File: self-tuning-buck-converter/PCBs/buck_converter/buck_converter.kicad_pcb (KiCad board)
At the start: 2 copper layers, 3 parts, among them U4 ESP32-DEVKITC-32D

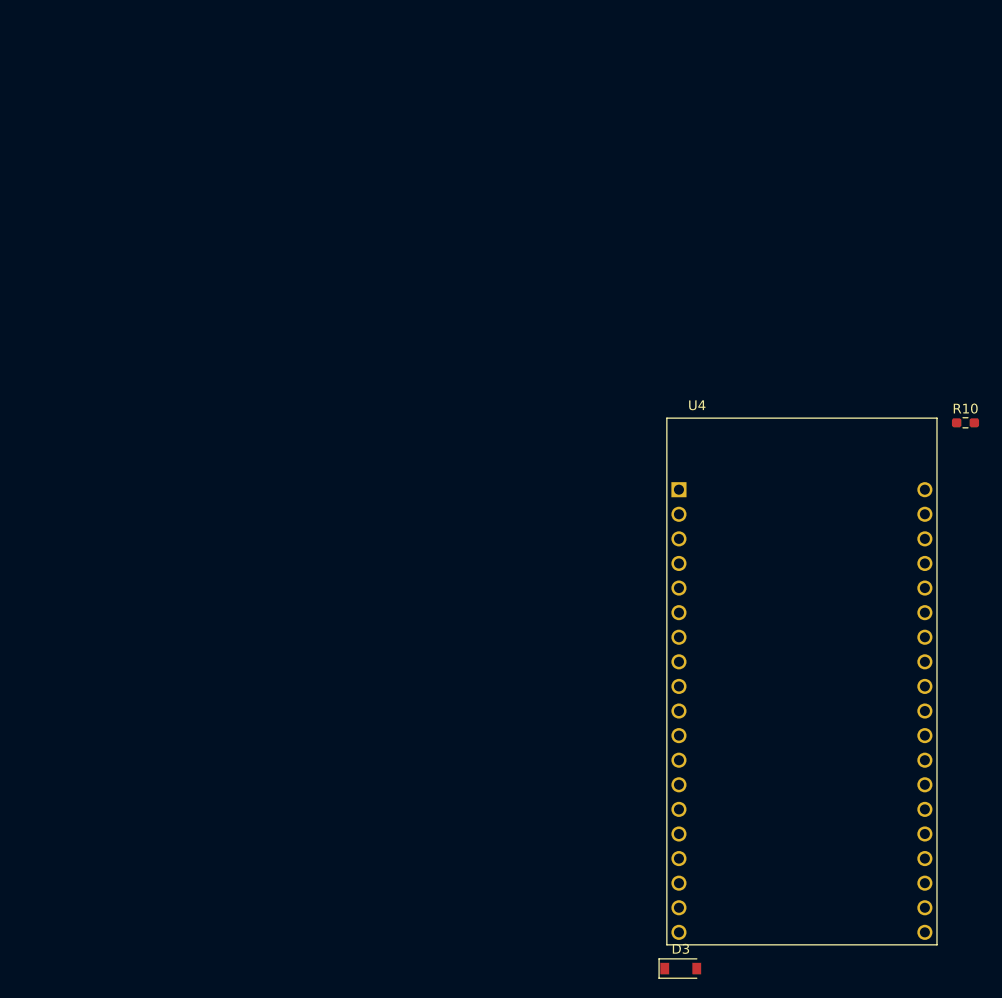
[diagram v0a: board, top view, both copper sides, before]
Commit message: Finalised PCM and selected component footprints
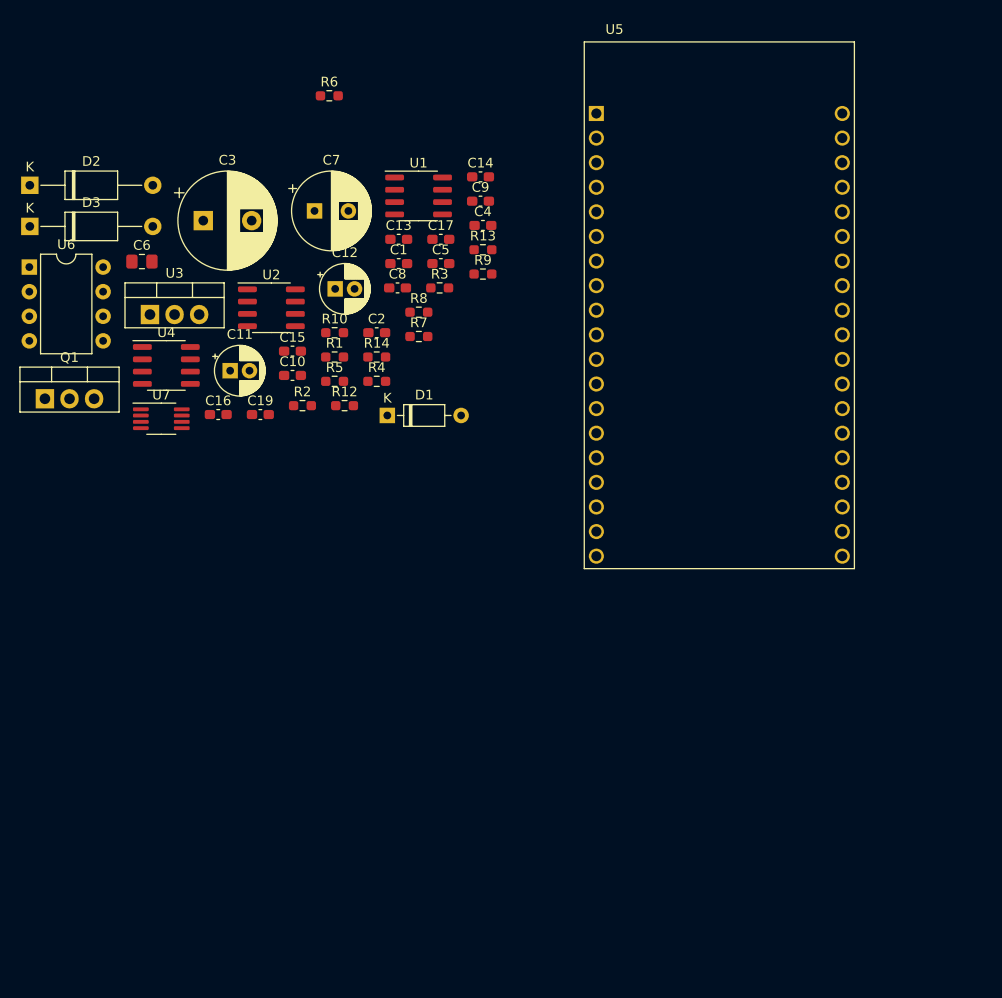
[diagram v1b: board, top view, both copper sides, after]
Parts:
- added C1: 0.1u 16V, Capacitor_SMD:C_0603_1608Metric_Pad1.08x0.95mm_HandSolder, F.Cu at (-33.1, -47.4)
- added C10: 1u 16V, Capacitor_SMD:C_0603_1608Metric_Pad1.08x0.95mm_HandSolder, F.Cu at (-44.1, -35.9)
- added C11: 10u 50V, Capacitor_THT:CP_Radial_D5.0mm_P2.00mm, F.Cu at (-50.5, -36.4)
- added C12: 10u 50V, Capacitor_THT:CP_Radial_D5.0mm_P2.00mm, F.Cu at (-39.7, -44.8)
- added C13: 0.1u 16V, Capacitor_SMD:C_0603_1608Metric_Pad1.08x0.95mm_HandSolder, F.Cu at (-33.1, -49.9)
- added C14: 0.1u 16V, Capacitor_SMD:C_0603_1608Metric_Pad1.08x0.95mm_HandSolder, F.Cu at (-24.7, -56.4)
- added C15: 0.1u 16V, Capacitor_SMD:C_0603_1608Metric_Pad1.08x0.95mm_HandSolder, F.Cu at (-44.1, -38.4)
- added C16: 0.1u 16V, Capacitor_SMD:C_0603_1608Metric_Pad1.08x0.95mm_HandSolder, F.Cu at (-51.8, -31.8)
- added C17: 4.7u 16V, Capacitor_SMD:C_0603_1608Metric_Pad1.08x0.95mm_HandSolder, F.Cu at (-28.8, -49.9)
- added C19: 0.1u 16V, Capacitor_SMD:C_0603_1608Metric_Pad1.08x0.95mm_HandSolder, F.Cu at (-47.4, -31.8)
- added C2: 0.1u 16V, Capacitor_SMD:C_0603_1608Metric_Pad1.08x0.95mm_HandSolder, F.Cu at (-35.4, -40.3)
- added C3: 100u 50V, Capacitor_THT:CP_Radial_D10.0mm_P5.00mm, F.Cu at (-53.3, -51.9)
- added C4: 0.1u 16V, Capacitor_SMD:C_0603_1608Metric_Pad1.08x0.95mm_HandSolder, F.Cu at (-24.4, -51.4)
- added C5: 100n 16V, Capacitor_SMD:C_0603_1608Metric_Pad1.08x0.95mm_HandSolder, F.Cu at (-28.8, -47.4)
- added C6: 10u 16V, Capacitor_SMD:C_0805_2012Metric_Pad1.18x1.45mm_HandSolder, F.Cu at (-59.6, -47.6)
- added C7: 100u 16V, Capacitor_THT:CP_Radial_D8.0mm_P3.50mm, F.Cu at (-41.8, -52.9)
- added C8: 0.1u 16V, Capacitor_SMD:C_0603_1608Metric_Pad1.08x0.95mm_HandSolder, F.Cu at (-33.2, -44.9)
- added C9: 10n 16V, Capacitor_SMD:C_0603_1608Metric_Pad1.08x0.95mm_HandSolder, F.Cu at (-24.7, -53.9)
- added D2: D_Schottky, Diode_THT:D_A-405_P12.70mm_Horizontal, F.Cu at (-71.2, -55.5)
- added D3: D_Schottky, Diode_THT:D_A-405_P12.70mm_Horizontal, F.Cu at (-71.2, -51.3)
- added Q1: NMOS, Package_TO_SOT_THT:TO-220-3_Vertical, F.Cu at (-69.7, -33.5)
- added R1: 100k, Resistor_SMD:R_0603_1608Metric_Pad0.98x0.95mm_HandSolder, F.Cu at (-39.7, -37.8)
- added R10: 120k, Resistor_SMD:R_0603_1608Metric_Pad0.98x0.95mm_HandSolder, F.Cu at (-39.7, -40.3)
- added R12: 5, Resistor_SMD:R_0603_1608Metric_Pad0.98x0.95mm_HandSolder, F.Cu at (-38.7, -32.8)
- added R13: 56k, Resistor_SMD:R_0603_1608Metric_Pad0.98x0.95mm_HandSolder, F.Cu at (-24.4, -48.9)
- added R14: 22k, Resistor_SMD:R_0603_1608Metric_Pad0.98x0.95mm_HandSolder, F.Cu at (-35.4, -37.8)
- added R2: 100k, Resistor_SMD:R_0603_1608Metric_Pad0.98x0.95mm_HandSolder, F.Cu at (-43.1, -32.8)
- added R3: 10k, Resistor_SMD:R_0603_1608Metric_Pad0.98x0.95mm_HandSolder, F.Cu at (-28.9, -44.9)
- added R4: 33, Resistor_SMD:R_0603_1608Metric_Pad0.98x0.95mm_HandSolder, F.Cu at (-35.4, -35.3)
- added R5: 1M, Resistor_SMD:R_0603_1608Metric_Pad0.98x0.95mm_HandSolder, F.Cu at (-39.7, -35.3)
- added R7: 10, Resistor_SMD:R_0603_1608Metric_Pad0.98x0.95mm_HandSolder, F.Cu at (-31.0, -39.9)
- added R8: 2k, Resistor_SMD:R_0603_1608Metric_Pad0.98x0.95mm_HandSolder, F.Cu at (-31.0, -42.4)
- added R9: 560k, Resistor_SMD:R_0603_1608Metric_Pad0.98x0.95mm_HandSolder, F.Cu at (-24.4, -46.4)
- added U1: LM7322, Package_SO:SOIC-8_3.9x4.9mm_P1.27mm, F.Cu at (-31.1, -54.4)
- added U2: LM7322, Package_SO:SOIC-8_3.9x4.9mm_P1.27mm, F.Cu at (-46.3, -42.9)
- added U3: LD1117V50, Package_TO_SOT_THT:TO-220-3_Vertical, F.Cu at (-58.8, -42.2)
- added U4: LT1999-50, Package_SO:SOIC-8_3.9x4.9mm_P1.27mm, F.Cu at (-57.1, -36.9)
- added U6: IR2125, Package_DIP:DIP-8_W7.62mm, F.Cu at (-71.3, -47.1)
- added U7: MAX11644, Package_SO:MSOP-8_3x3mm_P0.65mm, F.Cu at (-57.6, -31.4)
- D1: renamed from D3; footprint Diode_SMD:D_SOD-123 -> Diode_THT:D_DO-35_SOD27_P7.62mm_Horizontal
- moved R6 73.9 mm to (-40.3, -64.8)
- moved D1 64.7 mm to (-34.3, -31.8)
- moved U5 39.8 mm to (0.00, -43.2)
- renumbered R10 to R6, U4 to U5
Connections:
- U5 pad 10: Net-(U4-Pad10) -> SCL
- U5 pad 19: Net-(U4-Pad19) -> +5V
- U5 pad 5: Net-(U4-Pad5) -> Avg_voltage
- U5 pad 9: Net-(U4-Pad9) -> SDA

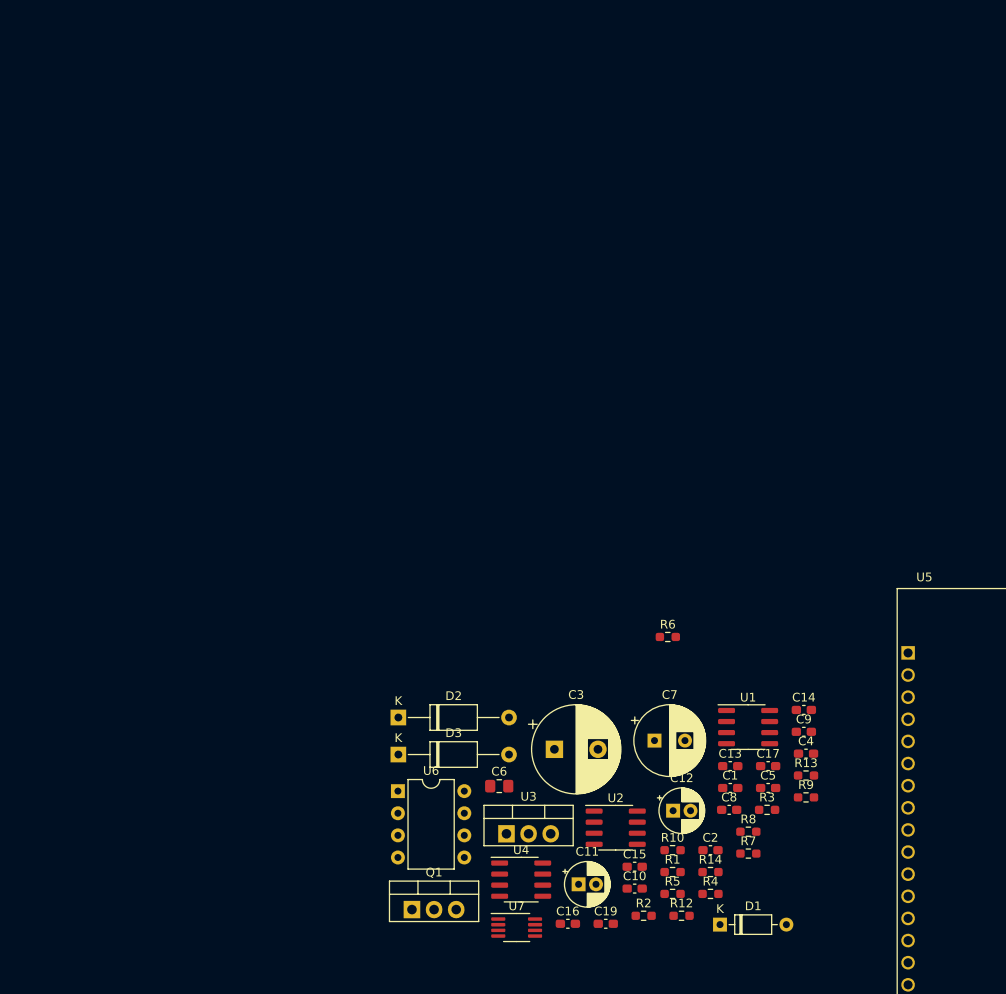
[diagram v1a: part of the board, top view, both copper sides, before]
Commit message: Updated schematic with edits found from building it in the lab
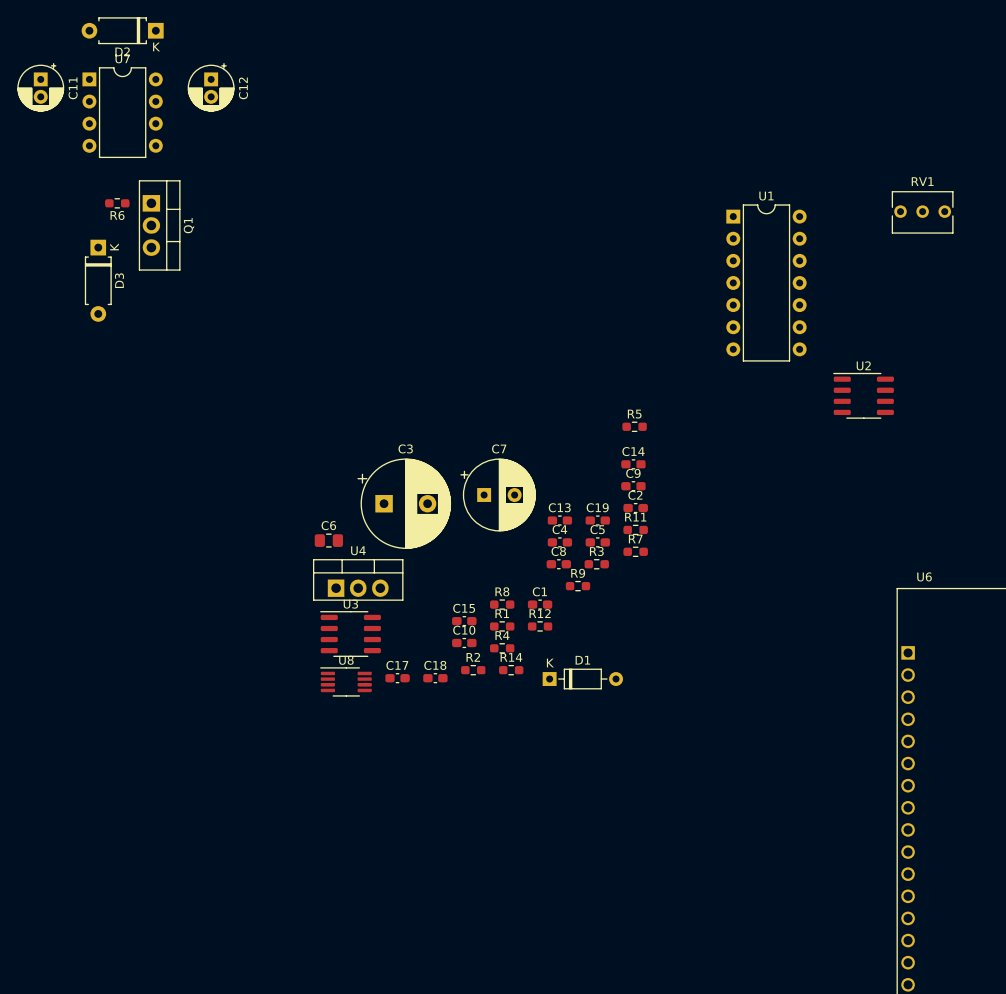
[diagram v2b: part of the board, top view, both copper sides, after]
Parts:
- removed the R4 at (-35.4, -35.3)
- removed the R6 at (-40.3, -64.8)
- removed the U2 at (-46.3, -42.9)
- added R5: 16k, Resistor_SMD:R_0603_1608Metric_Pad0.98x0.95mm_HandSolder, F.Cu at (-44.1, -88.9)
- added RV1: 100, Potentiometer_THT:Potentiometer_Bourns_3266Y_Vertical, F.Cu at (-8.49, -113.6)
- added U1: AMP from lab, Package_DIP:DIP-14_W7.62mm, F.Cu at (-32.8, -113.0)
- C9: value 10n 16V -> 100n 16V
- D2, D3: footprint Diode_THT:D_A-405_P12.70mm_Horizontal -> Diode_THT:D_A-405_P7.62mm_Horizontal
- moved C11 111.1 mm to (-112.3, -128.8), turned to 270 degrees
- moved R6 104.0 mm to (-103.5, -114.6), turned to 180 degrees
- moved C12 99.3 mm to (-92.7, -128.8), turned to 270 degrees
- moved U7 89.0 mm to (-106.7, -128.8)
- moved Q1 86.4 mm to (-99.6, -114.6), turned to 270 degrees
- moved D2 83.6 mm to (-99.1, -134.4), turned to 180 degrees
- moved D3 67.6 mm to (-105.7, -109.5), turned to 270 degrees
- moved U2 40.3 mm to (-17.8, -92.5)
- moved C1 34.3 mm to (-54.9, -68.5)
- moved R8 34.3 mm to (-59.3, -68.5)
- moved C10 34.3 mm to (-63.6, -64.1)
- moved C13 34.3 mm to (-52.7, -78.1)
- moved C14 34.3 mm to (-44.2, -84.6)
- moved C15 34.3 mm to (-63.6, -66.6)
- moved C17 34.3 mm to (-71.3, -60.0)
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- renumbered C2 to C1, C16 to C17, C19 to C18, C17 to C19, C4 to C2, C1 to C4, R13 to R11, R14 to R12, R12 to R14, R5 to R4, R7 to R6, R9 to R7, R10 to R8, R8 to R9, U1 to U2, U4 to U3, U3 to U4, U5 to U6, U6 to U7, U7 to U8
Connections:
- C11 pad 1: GND -> +12V
- C11 pad 2: +12V -> GND
- D3 pad 1: Net-(D3-Pad1) -> Net-(C12-Pad2)
- Q1 pad 3: Net-(D3-Pad1) -> Net-(C12-Pad2)
- U2 pad 5: Net-(C9-Pad2) -> (no net)
- U2 pad 6: Pk_voltage -> (no net)
- U2 pad 7: Pk_voltage -> (no net)
